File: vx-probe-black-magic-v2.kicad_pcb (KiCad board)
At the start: 2 copper layers, 72.4 x 41.9 mm, 44 parts, among them P1 USB MINI B, P10 CONN_01X01, P11 CONN_01X11, P12 CONN_01X03, P2 +5v power input, P3 +5v external input, P4 CONN_02X05, P5 CONN_01X04, P6 swdio/jtag, P7 CONN_01X01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

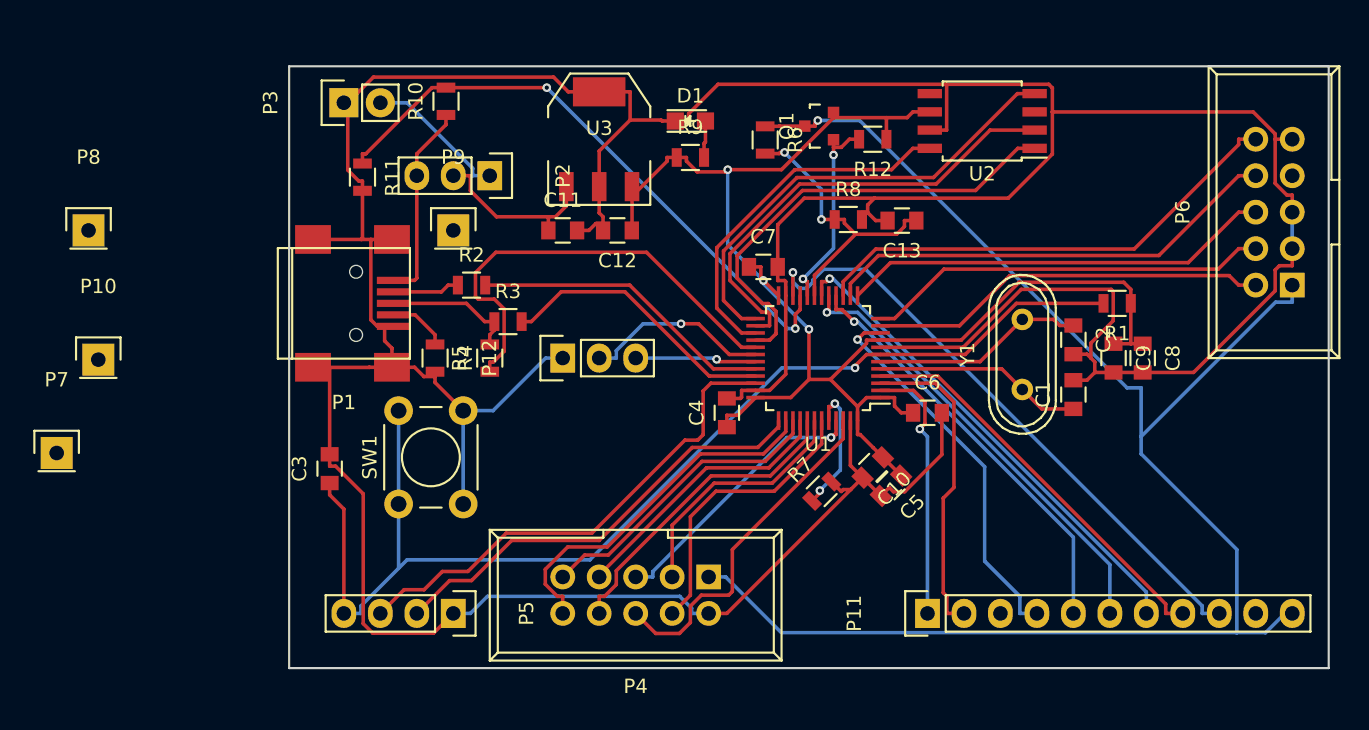
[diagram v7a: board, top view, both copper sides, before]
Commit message: made the power-to-target tracks thicker
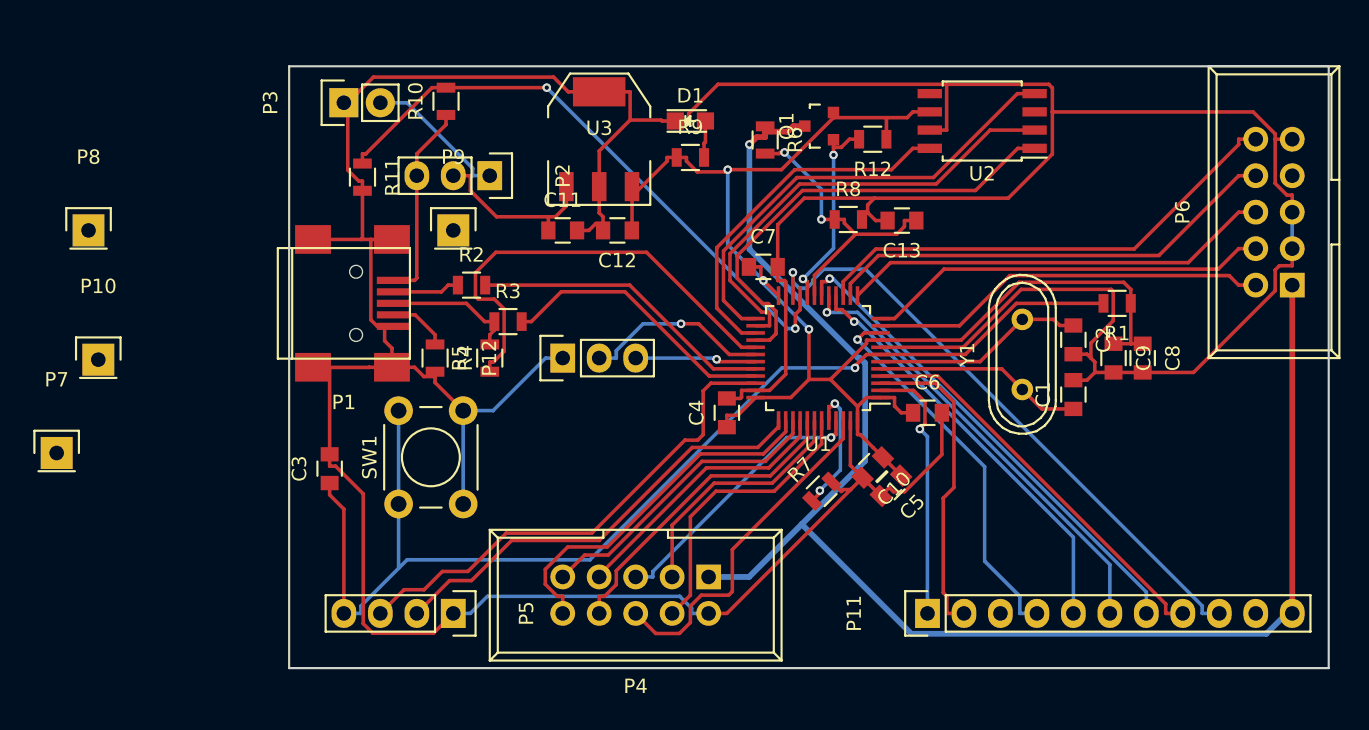
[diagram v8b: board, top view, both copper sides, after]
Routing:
- net /TPWR: track 112.4 -> 105.6 mm
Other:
- net class POWER_TO_TARGET added: clearance 0.2, trace_width 0.4, via_dia 0.6, via_drill 0.4
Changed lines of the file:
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@@
     (thickness 1.6)
     (drawings 11)
-    (tracks 574)
+    (tracks 573)
     (zones 0)
     (modules 44)
@@
     (add_net /SWO/TDO)
     (add_net /TDI)
-    (add_net /TPWR)
     (add_net /TPWR_CTRL)
     (add_net /TPWR_IN)
@@
     (add_net "Net-(U2-Pad3)")
     (add_net "Net-(U2-Pad5)")
+  )
+  (net_class POWER_TO_TARGET ""
+    (clearance 0.2)
+    (trace_width 0.4)
+    (via_dia 0.6)
+    (via_drill 0.4)
+    (uvia_dia 0.3)
+    (uvia_drill 0.1)
+    (add_net /TPWR)
   )
   (module Connect:IDC_Header_Straight_10pins (layer F.Cu)
@@
   (segment (start 93.7935 58.44) (end 97.8196 54.4139) (width 0.25) (layer F.Cu) (net 4))
   (segment (start 88.17 58.44) (end 93.7935 58.44) (width 0.25) (layer F.Cu) (net 4))
+  (segment (start 86.57 63.0647) (end 84.6814 61.1761) (width 0.25) (layer F.Cu) (net 4))
+  (segment (start 84.6814 61.1761) (end 83.185 61.1761) (width 0.25) (layer F.Cu) (net 4))
   (segment (start 104.394 58.69) (end 105.598 58.69) (width 0.25) (layer F.Cu) (net 4))
   (segment (start 105.598 58.69) (end 106.426 58.69) (width 0.25) (layer F.Cu) (net 4))
-  (segment (start 86.57 63.0647) (end 84.6814 61.1761) (width 0.25) (layer F.Cu) (net 4))
-  (segment (start 84.6814 61.1761) (end 83.185 61.1761) (width 0.25) (layer F.Cu) (net 4))
   (segment (start 57.5948 55.0799) (end 54.2493 55.0799) (width 0.25) (layer F.Cu) (net 5))
   (segment (start 58.0647 54.61) (end 57.5948 55.0799) (width 0.25) (layer F.Cu) (net 5))
@@
   (segment (start 85.6535 50.038) (end 85.6535 50.2912) (width 0.25) (layer F.Cu) (net 51))
   (segment (start 84.9782 50.038) (end 85.6535 50.038) (width 0.25) (layer F.Cu) (net 51))
-  (via (at 83.7987 43.1457) (size 0.6) (layers F.Cu B.Cu) (net 53))
-  (segment (start 81.1275 43.5356) (end 82.898 43.5356) (width 0.25) (layer F.Cu) (net 53))
-  (segment (start 81.1123 43.5508) (end 81.1275 43.5356) (width 0.25) (layer F.Cu) (net 53))
-  (segment (start 80.137 43.5508) (end 81.1123 43.5508) (width 0.25) (layer F.Cu) (net 53))
-  (segment (start 83.6233 43.3211) (end 83.7987 43.1457) (width 0.25) (layer F.Cu) (net 53))
-  (segment (start 83.6233 43.5356) (end 83.6233 43.3211) (width 0.25) (layer F.Cu) (net 53))
-  (segment (start 82.898 43.5356) (end 83.6233 43.5356) (width 0.25) (layer F.Cu) (net 53))
-  (segment (start 114.986 78.8114) (end 112.978 78.8114) (width 0.25) (layer B.Cu) (net 53))
-  (segment (start 116.328 77.47) (end 114.986 78.8114) (width 0.25) (layer B.Cu) (net 53))
-  (segment (start 116.84 77.47) (end 116.328 77.47) (width 0.25) (layer B.Cu) (net 53))
-  (segment (start 77.3889 74.93) (end 76.2 74.93) (width 0.25) (layer B.Cu) (net 53))
-  (segment (start 81.2703 78.8114) (end 77.3889 74.93) (width 0.25) (layer B.Cu) (net 53))
-  (segment (start 112.978 78.8114) (end 81.2703 78.8114) (width 0.25) (layer B.Cu) (net 53))
-  (segment (start 106.319 66.3622) (end 106.319 65.158) (width 0.25) (layer B.Cu) (net 53))
-  (segment (start 112.978 73.0208) (end 106.319 66.3622) (width 0.25) (layer B.Cu) (net 53))
-  (segment (start 112.978 78.8114) (end 112.978 73.0208) (width 0.25) (layer B.Cu) (net 53))
-  (segment (start 86.7201 43.1457) (end 83.7987 43.1457) (width 0.25) (layer B.Cu) (net 53))
-  (segment (start 105.333 61.759) (end 86.7201 43.1457) (width 0.25) (layer B.Cu) (net 53))
-  (segment (start 106.319 61.759) (end 105.333 61.759) (width 0.25) (layer B.Cu) (net 53))
-  (segment (start 106.319 65.158) (end 106.319 61.759) (width 0.25) (layer B.Cu) (net 53))
-  (segment (start 115.678 55.7989) (end 106.319 65.158) (width 0.25) (layer B.Cu) (net 53))
-  (segment (start 116.84 55.7989) (end 115.678 55.7989) (width 0.25) (layer B.Cu) (net 53))
-  (segment (start 116.84 54.61) (end 116.84 55.7989) (width 0.25) (layer B.Cu) (net 53))
+  (via (at 79.0385 44.8146) (size 0.6) (layers F.Cu B.Cu) (net 53))
+  (segment (start 116.84 77.47) (end 116.84 54.61) (width 0.4) (layer F.Cu) (net 53))
+  (segment (start 90.3079 78.8864) (end 82.6838 71.2623) (width 0.4) (layer B.Cu) (net 53))
+  (segment (start 115.04 78.8864) (end 90.3079 78.8864) (width 0.4) (layer B.Cu) (net 53))
+  (segment (start 116.456 77.47) (end 115.04 78.8864) (width 0.4) (layer B.Cu) (net 53))
+  (segment (start 79.0161 74.93) (end 76.2 74.93) (width 0.4) (layer B.Cu) (net 53))
+  (segment (start 82.6838 71.2623) (end 79.0161 74.93) (width 0.4) (layer B.Cu) (net 53))
+  (segment (start 87.0978 66.8483) (end 82.6838 71.2623) (width 0.4) (layer B.Cu) (net 53))
+  (segment (start 87.0978 60.0442) (end 87.0978 66.8483) (width 0.4) (layer B.Cu) (net 53))
+  (segment (start 86.7258 59.6722) (end 87.0978 60.0442) (width 0.4) (layer B.Cu) (net 53))
+  (segment (start 86.6019 59.6722) (end 86.7258 59.6722) (width 0.4) (layer B.Cu) (net 53))
+  (segment (start 79.0385 52.1088) (end 86.6019 59.6722) (width 0.4) (layer B.Cu) (net 53))
+  (segment (start 79.0385 44.8146) (end 79.0385 52.1088) (width 0.4) (layer B.Cu) (net 53))
+  (segment (start 80.137 43.5508) (end 80.137 43.9259) (width 0.4) (layer F.Cu) (net 53))
+  (segment (start 79.552 44.3011) (end 79.0385 44.8146) (width 0.4) (layer F.Cu) (net 53))
+  (segment (start 80.137 44.3011) (end 79.552 44.3011) (width 0.4) (layer F.Cu) (net 53))
+  (segment (start 80.137 43.9259) (end 80.137 44.3011) (width 0.4) (layer F.Cu) (net 53))
+  (segment (start 81.7073 43.9259) (end 80.137 43.9259) (width 0.4) (layer F.Cu) (net 53))
+  (segment (start 82.0976 43.5356) (end 81.7073 43.9259) (width 0.4) (layer F.Cu) (net 53))
+  (segment (start 82.898 43.5356) (end 82.0976 43.5356) (width 0.4) (layer F.Cu) (net 53))
+  (segment (start 116.84 77.47) (end 116.456 77.47) (width 0.25) (layer B.Cu) (net 53))
+  (segment (start 116.456 77.47) (end 116.328 77.47) (width 0.25) (layer B.Cu) (net 53))
   (via (at 82.2369 57.6337) (size 0.6) (layers F.Cu B.Cu) (net 54))
   (via (at 64.9285 40.8584) (size 0.6) (layers F.Cu B.Cu) (net 54))
